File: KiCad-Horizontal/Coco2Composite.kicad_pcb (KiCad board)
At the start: 2 copper layers, 52 x 36.5 mm, 20 parts, among them J1 MA03-1, J2 MA05-1, J3 AUDIO_JACK_3.5MM_PTH, Q1 PN2907, Q2 2N2222, U1 MC1372

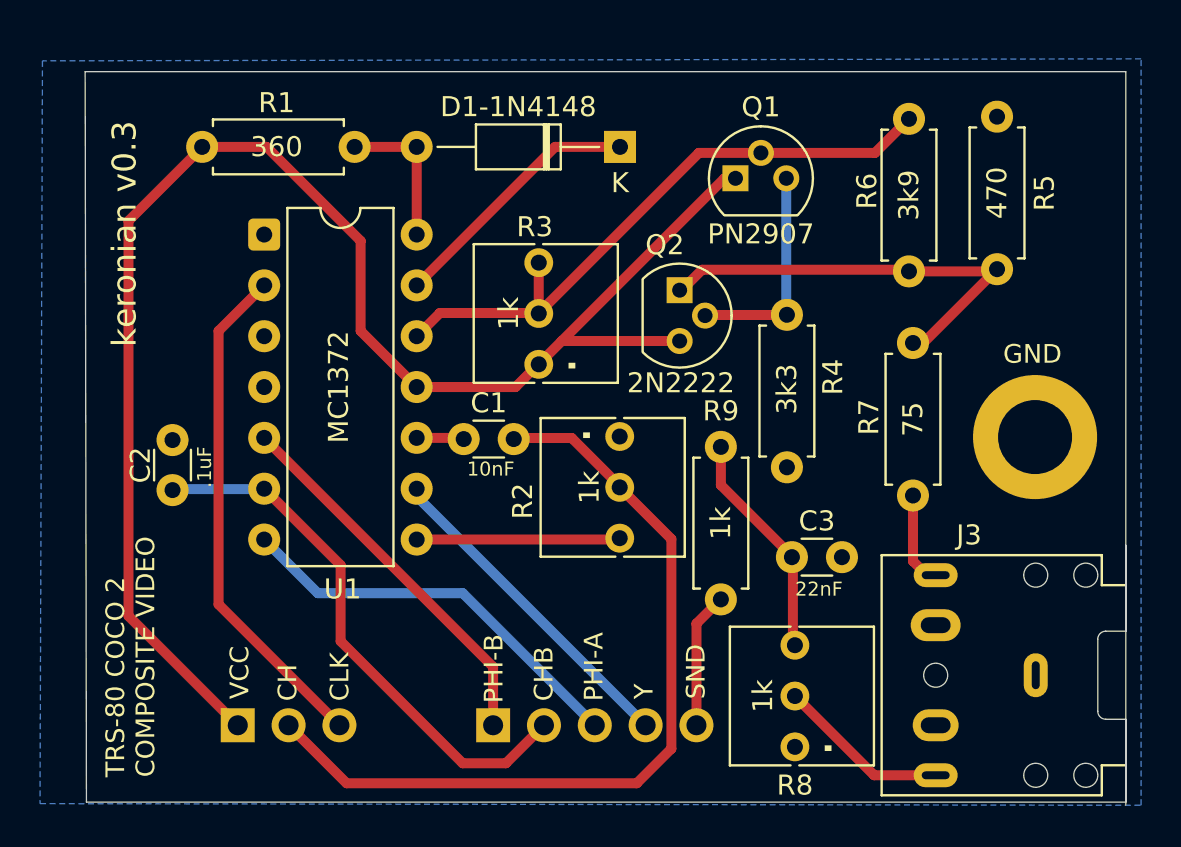
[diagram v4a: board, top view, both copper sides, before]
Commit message: Reworked traces to keep them all on the front, shrunk trace width to 0.25
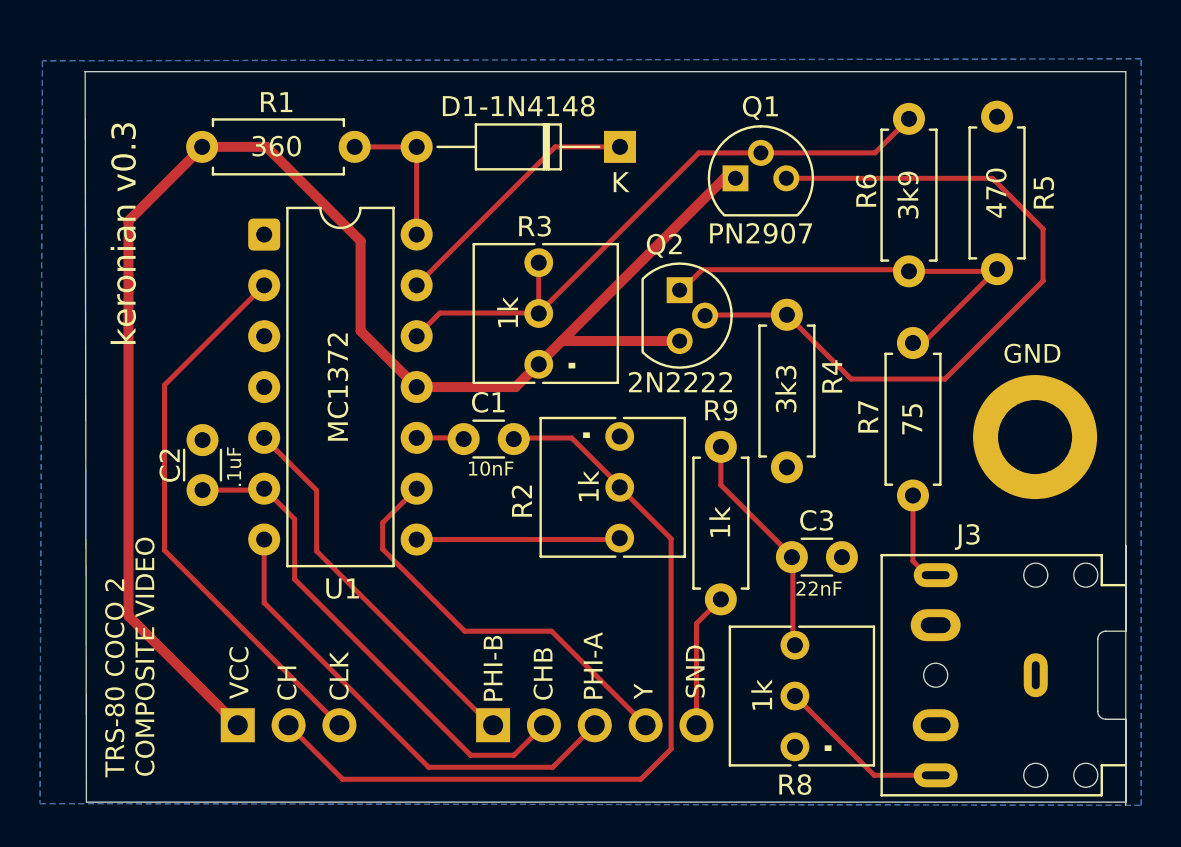
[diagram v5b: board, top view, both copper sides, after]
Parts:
- moved C2 1.50 mm to (121.9, 109.2)
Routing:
- net /Q1_E: track 10.9 -> 36.7 mm
- net /Y: track 16.6 -> 20.5 mm
- net /PHI-A: track 20.4 -> 24.0 mm
- net /CHB: track 27.3 -> 25.0 mm
- net /CLK: track 25.4 -> 27.7 mm

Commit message: Added a supply bypass capacitor
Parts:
- added C4: 1uF, Capacitor_THT:C_Disc_D3.0mm_W1.6mm_P2.50mm, F.Cu at (119.1, 99.1)
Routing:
- net VCC: track 77.2 -> 76.4 mm
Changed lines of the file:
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@@
+		)
+	)
+	(footprint "Capacitor_THT:C_Disc_D3.0mm_W1.6mm_P2.50mm"
+		(layer "F.Cu")
+		(at 119.131248 99.079329)
+		(descr "C, Disc series, Radial, pin pitch=2.50mm, diameter*width=3.0*1.6mm^2, Capacitor, http://www.vishay.com/docs/45233/krseries.pdf")
+		(tags "C Disc series Radial pin pitch 2.50mm diameter 3.0mm width 1.6mm Capacitor")
+		(property "Reference" "C4"
+			(at 1.25 -1.6 0)
+			(layer "F.SilkS")
+			(effects
+				(font
+					(size 1 1)
+					(thickness 0.15)
+				)
+			)
+		)
+		(property "Value" "1uF"
+			(at 1.15 1.6 0)
+			(layer "F.SilkS")
+			(effects
+				(font
+					(size 0.7 0.7)
+					(thickness 0.0875)
+				)
+			)
+		)
+		(property "Datasheet" ""
+			(at 0 0 0)
+			(layer "F.Fab")
+			(hide yes)
+			(effects
+				(font
+					(size 1.27 1.27)
+					(thickness 0.15)
+				)
+			)
+		)
+		(property "Description" "capacitor, small US symbol"
+			(at 0 0 0)
+			(layer "F.Fab")
+			(hide yes)
+			(effects
+				(font
+					(size 1.27 1.27)
+					(thickness 0.15)
+				)
+			)
+		)
+		(attr through_hole)
+		(fp_line
+			(start 0.485 -0.92)
+			(end 2.015 -0.92)
+			(stroke
+				(width 0.12)
+				(type solid)
+			)
+			(layer "F.SilkS")
+		)
+		(fp_line
+			(start 0.485 0.92)
+			(end 2.015 0.92)
+			(stroke
+				(width 0.12)
+				(type solid)
+			)
+			(layer "F.SilkS")
+		)
+		(fp_line
+			(start -1.05 -1.05)
+			(end -1.05 1.05)
+			(stroke
+				(width 0.05)
+				(type solid)
+			)
+			(layer "F.CrtYd")
+		)
+		(fp_line
+			(start -1.05 1.05)
+			(end 3.55 1.05)
+			(stroke
+				(width 0.05)
+				(type solid)
+			)
+			(layer "F.CrtYd")
+		)
+		(fp_line
+			(start 3.55 -1.05)
+			(end -1.05 -1.05)
+			(stroke
+				(width 0.05)
+				(type solid)
+			)
+			(layer "F.CrtYd")
+		)
+		(fp_line
+			(start 3.55 1.05)
+			(end 3.55 -1.05)
+			(stroke
+				(width 0.05)
+				(type solid)
+			)
+			(layer "F.CrtYd")
+		)
+		(fp_line
+			(start -0.25 -0.8)
+			(end -0.25 0.8)
+			(stroke
+				(width 0.1)
+				(type solid)
+			)
+			(layer "F.Fab")
+		)
+		(fp_line
+			(start -0.25 0.8)
+			(end 2.75 0.8)
+			(stroke
+				(width 0.1)
+				(type solid)
+			)
+			(layer "F.Fab")
+		)
+		(fp_line
+			(start 2.75 -0.8)
+			(end -0.25 -0.8)
+			(stroke
+				(width 0.1)
+				(type solid)
+			)
+			(layer "F.Fab")
+		)
+		(fp_line
+			(start 2.75 0.8)
+			(end 2.75 -0.8)
+			(stroke
+				(width 0.1)
+				(type solid)
+			)
+			(layer "F.Fab")
+		)
+		(fp_text user "${REFERENCE}"
+			(at 1.25 0 0)
+			(layer "F.Fab")
+			(effects
+				(font
+					(size 0.6 0.6)
+					(thickness 0.09)
+				)
+			)
+		)
+		(pad "1" thru_hole circle
+			(at 0 0)
+			(size 1.6 1.6)
+			(drill 0.8)
+			(layers "*.Cu" "*.Mask")
+			(remove_unused_layers no)
+			(net 1 "VCC")
+			(pintype "passive")
+		)
+		(pad "2" thru_hole circle
+			(at 2.5 0)
+			(size 1.6 1.6)
+			(drill 0.8)
+			(layers "*.Cu" "*.Mask")
+			(remove_unused_layers no)
+			(net 2 "GND")
+			(pintype "passive")
+		)
+		(embedded_fonts no)
+		(model "${KICAD9_3DMODEL_DIR}/Capacitor_THT.3dshapes/C_Disc_D3.0mm_W1.6mm_P2.50mm.wrl"
+			(offset
+				(xyz 0 0 0)
+			)
+			(scale
+				(xyz 1 1 1)
+			)
+			(rotate
+				(xyz 0 0 0)
+			)
 		)
 	)
@@
 	)
 	(gr_text "keronian v0.3"
-		(at 118.7 102.1 90)
+		(at 118.1 102 90)
 		(layer "F.SilkS")
 		(effects
@@
 	)
 	(segment
+		(start 132.6 104.1)
+		(end 137.54 104.1)
+		(width 0.5)
+		(layer "F.Cu")
+		(net 1)
+	)
+	(segment
+		(start 123.66 121)
+		(end 119.1 116.44)
+		(width 0.5)
+		(layer "F.Cu")
+		(net 1)
+	)
+	(segment
+		(start 119.1 116.44)
+		(end 119.1 94.9)
+		(width 0.5)
+		(layer "F.Cu")
+		(net 1)
+	)
+	(segment
+		(start 147.98 93.67)
+		(end 138.71 102.94)
+		(width 0.5)
+		(layer "F.Cu")
+		(net 1)
+	)
+	(segment
+		(start 137.54 104.1)
+		(end 138.7 102.94)
+		(width 0.5)
+		(layer "F.Cu")
+		(net 1)
+	)
+	(segment
+		(start 139.84 101.8)
+		(end 145.74 101.8)
+		(width 0.5)
+		(layer "F.Cu")
+		(net 1)
+	)
+	(segment
+		(start 148.53 93.67)
+		(end 147.98 93.67)
+		(width 0.5)
+		(layer "F.Cu")
+		(net 1)
+	)
+	(segment
+		(start 125.1 92.1)
+		(end 129.8 96.8)
+		(width 0.5)
+		(layer "F.Cu")
+		(net 1)
+	)
+	(segment
+		(start 119.1 94.9)
+		(end 121.9 92.1)
+		(width 0.5)
+		(layer "F.Cu")
+		(net 1)
+	)
+	(segment
+		(start 129.8 96.8)
+		(end 129.8 101.3)
+		(width 0.5)
+		(layer "F.Cu")
+		(net 1)
+	)
+	(segment
+		(start 129.8 101.3)
+		(end 132.6 104.1)
+		(width 0.5)
+		(layer "F.Cu")
+		(net 1)
+	)
+	(segment
 		(start 121.9 92.1)
 		(end 125.1 92.1)
@@
 	)
 	(segment
-		(start 132.6 104.1)
-		(end 137.54 104.1)
-		(width 0.5)
-		(layer "F.Cu")
-		(net 1)
-	)
-	(segment
-		(start 129.8 96.8)
-		(end 129.8 101.3)
-		(width 0.5)
-		(layer "F.Cu")
-		(net 1)
-	)
-	(segment
-		(start 118.2 95.8)
-		(end 121.9 92.1)
-		(width 0.5)
-		(layer "F.Cu")
-		(net 1)
-	)
-	(segment
-		(start 123.66 121)
-		(end 118.2 115.54)
-		(width 0.5)
-		(layer "F.Cu")
-		(net 1)
-	)
-	(segment
-		(start 118.2 115.54)
-		(end 118.2 95.8)
-		(width 0.5)
-		(layer "F.Cu")
-		(net 1)
-	)
-	(segment
-		(start 129.8 101.3)
-		(end 132.6 104.1)
-		(width 0.5)
-		(layer "F.Cu")
-		(net 1)
-	)
-	(segment
-		(start 125.1 92.1)
-		(end 129.8 96.8)
-		(width 0.5)
-		(layer "F.Cu")
-		(net 1)
-	)
-	(segment
-		(start 147.98 93.67)
-		(end 138.71 102.94)
-		(width 0.5)
-		(layer "F.Cu")
-		(net 1)
-	)
-	(segment
-		(start 137.54 104.1)
-		(end 138.7 102.94)
-		(width 0.5)
-		(layer "F.Cu")
-		(net 1)
-	)
-	(segment
-		(start 139.84 101.8)
-		(end 145.74 101.8)
-		(width 0.5)
-		(layer "F.Cu")
-		(net 1)
-	)
-	(segment
-		(start 148.53 93.67)
-		(end 147.98 93.67)
-		(width 0.5)
-		(layer "F.Cu")
-		(net 1)
-	)
-	(segment
 		(start 124.91 109.25)
 		(end 124.98 109.18)
@@
 	(segment
 		(start 128.74 121)
-		(end 120 112.26)
+		(end 120.3 112.56)
 		(width 0.25)
 		(layer "F.Cu")
@@
 	)
 	(segment
-		(start 120 104)
+		(start 120.3 103.7)
 		(end 124.98 99.02)
 		(width 0.25)
@@
 	)
 	(segment
-		(start 120 112.26)
-		(end 120 104)
-		(width 0.25)
-		(layer "F.Cu")
+		(start 120.3 112.56)
+		(end 120.3 103.7)
+		(width 0.25)
+		(layer "F.Cu")
